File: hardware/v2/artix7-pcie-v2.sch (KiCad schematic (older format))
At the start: 34 parts, among them J10 USB_B_Micro, J3 JTAG_EN, J6 JTAG, J7 Conn_01x02, J8 SER0, J9 SER1, SW1 PROG, SW2 SW_SPST, U1 XC7A75T-FGG484, U2 W25Q64JVSSIM

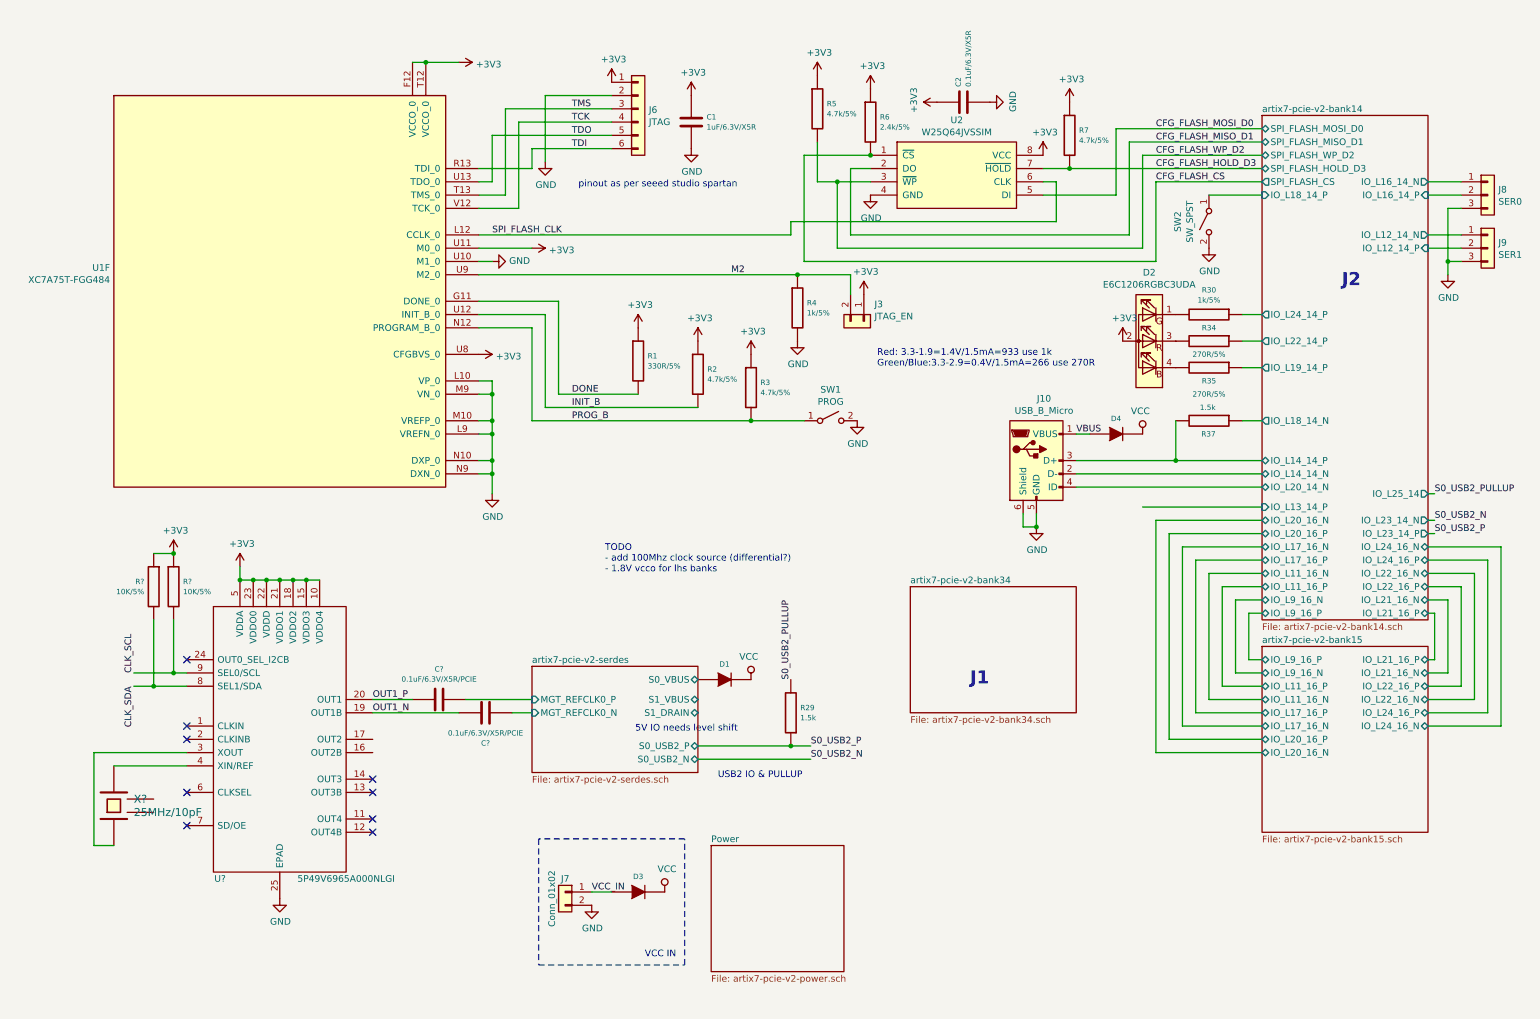
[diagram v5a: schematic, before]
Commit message: v2 pcb/schematic update : drc passing, need to add caps
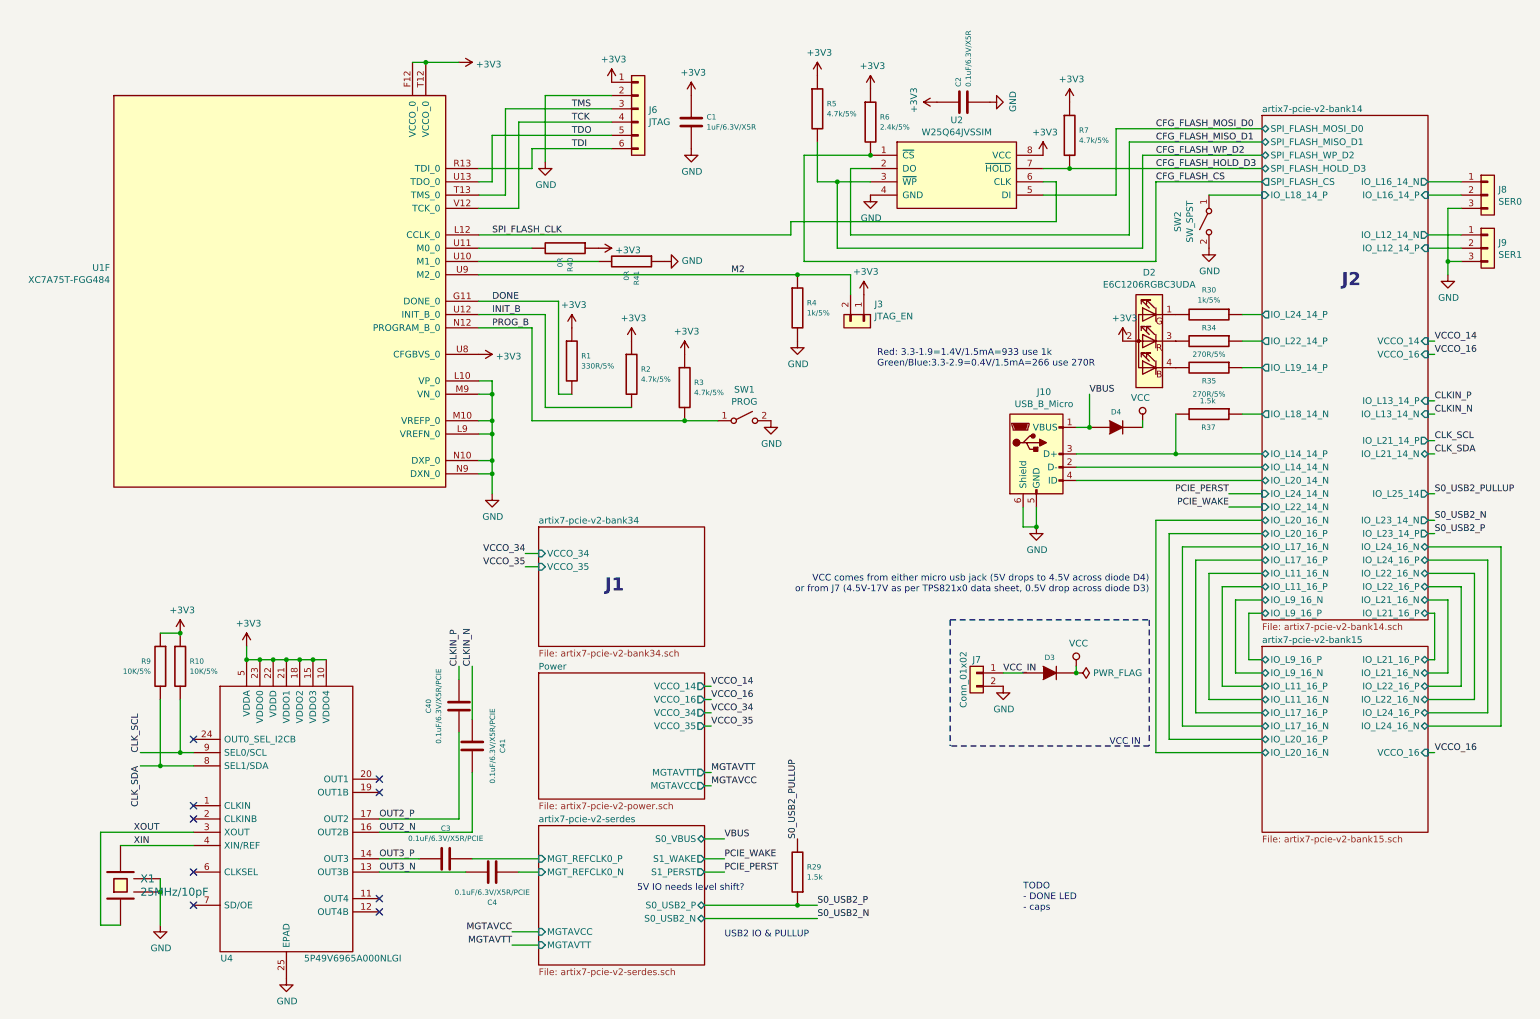
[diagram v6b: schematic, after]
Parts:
- removed D1: SBR3U20SA-13‎, tom-semiconductors:D_SMA, symbol tom-passives:DIODE
- added C40, C41: 0.1uF/6.3V/X5R/PCIE, tom-passives:C_0402_1005Metric, symbol tom-passives:C
- added R40, R41: 0R, tom-passives:C_0402_1005Metric, symbol tom-passives:R
- J6: footprint tom-connectors:PinHeader_1x06_P2.54mm_Vertical_SMD_Pin1Left -> tom-connectors:PinHeader_2x03_P2.54mm_Vertical
- U4: renamed from U?; footprint QFN50P400X400X100-25N-D -> artix7-pcie-v2:QFN50P400X400X100-25N-D
- gave numbers to parts that had none: 5
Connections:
- net +3V3: now also R40.1; no longer U1.U11 (M0_0)
- net GND: now also X1.2 (GND), X1.4 (GND), R41.1; no longer U1.U10 (M1_0)
- net OUT3_N: now reaches U4.13 (OUT3B)
- net OUT3_N: now also C4.1
- net OUT3_P: now reaches U4.14 (OUT3)
- net OUT3_P: now also C3.2
- net OUT2_N: now reaches U4.16 (OUT2B)
- net OUT2_N: now also C41.1
- net OUT2_P: now reaches U4.17 (OUT2)
- net OUT2_P: now also C40.2
- net XOUT: now reaches U4.3 (XOUT), X1.1
- net XIN: now reaches U4.4 (XIN/REF), X1.3
- net OUT1_N: no longer names the net of U4.19 (OUT1B)
- net OUT1_N: no longer C4.1
- net OUT1_P: no longer names the net of U4.20 (OUT1)
- net OUT1_P: no longer C3.2
- new net: R41.2, U1.U10 (M1_0)
- new net: R40.2, U1.U11 (M0_0)
- new net CLKIN_N: C41.2
- new net CLKIN_P: C40.1
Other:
- note added: "5V IO needs level shift?"
- note added: "TODO \n- DONE LED\n- caps"
- note added: "VCC comes from either micro usb jack (5V drops to 4.5V across diode D4)\nor from J7 (4.5V-17V as per TPS821x0 data sheet, 0.5V drop across diode D3)"
- note removed: "5V IO needs level shift"
- note removed: "TODO \n- add 100Mhz clock source (differential?)\n- 1.8V vcco for lhs banks"
- note removed: "pinout as per seeed studio spartan"
- moved on the sheet: C3, C4, D3, D4, J10, J7, R1, R10, R2, R29, R3, R37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

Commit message: v2 hardware: pcb progress commit, 155 unrouted
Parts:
- removed J8: SER0, tom-connectors:PinHeader_1x03_P2.54mm_Vertical, symbol tom-connectors:Conn_01x03
- removed J9: SER1, tom-connectors:PinHeader_1x03_P2.54mm_Vertical, symbol tom-connectors:Conn_01x03
- removed R40, R41: 0R, tom-passives:C_0402_1005Metric, symbol tom-passives:R
- added C17, C25, C27, C29, C31: 0.1uF/6.3V/X5R, tom-passives:C_0402_1005Metric, symbol tom-passives:C
- added D1: DONE, tom-passives:C_0402_1005Metric, symbol tom-opto:LED
- added D5: PWR, tom-passives:C_0402_1005Metric, symbol tom-opto:LED
- added J8: SER, tom-connectors:PinHeader_2x03_P2.54mm_Vertical, symbol tom-connectors:Conn_01x06
- added R51: 1K/5%, tom-passives:C_0402_1005Metric, symbol tom-passives:R
- added TP9: TestPoint, tom-mechanical:TestPoint_Loop_D2.50mm_Drill1.0mm, symbol tom-mechanical:TestPoint
- C1: value 1uF/6.3V/X5R -> 47uF/6.3V/X5R; footprint tom-passives:C_0402_1005Metric -> tom-passives:C_1206_3216Metric
- R1: value 330R/5% -> 1K/5%
- U2: footprint tom-semiconductors:SOIC-8_5.23x5.23mm_P1.27mm -> artix7-pcie-v2:WSON-8-1EP_8x6mm_P1.27mm
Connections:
- net +3V3: now also U1.U11 (M0_0), C17.1, C25.1, C27.1, C29.1, C31.1, R51.1
- net CLKIN_P: now also C40.2; no longer C40.1
- net DONE: now also D1.2 (A)
- net GND: now also U1.U10 (M1_0), C17.2, C25.2, C27.2, C29.2, C31.2, D1.1 (K), D5.1 (K), J8.1 (Pin_1), J8.2 (Pin_2), TP9.1
- net OUT2_P: now also C40.1; no longer C40.2
- net OUT3_P: now also C3.1; no longer C3.2
- net artix7-pcie-v2-bank14/IO_L12_14_N: now also J8.5 (Pin_5)
- net artix7-pcie-v2-bank14/IO_L12_14_P: now also J8.6 (Pin_6)
- net artix7-pcie-v2-bank14/IO_L16_14_N: now also J8.3 (Pin_3)
- net artix7-pcie-v2-bank14/IO_L16_14_P: now also J8.4 (Pin_4)
- net artix7-pcie-v2-serdes/MGT_REFCLK0_P: now also C3.2; no longer C3.1
- net artix7-pcie-v2-bank14/IO_L20_14_N renamed artix7-pcie-v2-bank14/IO_L11_14_P
- new net: D5.2 (A), R51.2
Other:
- note added: "Red Yeti Artix7 PCIe"
- note added: "TODO \n- POWER Good led\n- VCC led ?\n- caps for connectors (J1 and J2)\n- ps caps for clock chip"
- note added: "VCC comes from either micro usb jack (5V drops to approx 4V across diode D4)\nor from J7 (4V-17V as per TPS821x0 data sheet, 1V drop across diode D3)"
- note removed: "5V IO needs level shift?"
- note removed: "TODO \n- DONE LED\n- caps"
- note removed: "VCC comes from either micro usb jack (5V drops to 4.5V across diode D4)\nor from J7 (4.5V-17V as per TPS821x0 data sheet, 0.5V drop across diode D3)"
- moved on the sheet: C1

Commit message: v2 pcb/schematic progress commit, all tough signals routed out
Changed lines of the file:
@@
 F7 "MGTAVTT" I L 3900 7250 50
 F8 "MGTAVCC" I L 3900 7150 50
-F9 "S3_PERST" O R 5150 6700 50
-F10 "S3_WAKE" O R 5150 6600 50
+F9 "S2_PERST" O R 5150 6700 50
+F10 "S2_WAKE" O R 5150 6600 50
 $EndSheet
 Text Notes 5300 7200 0    50   ~ 0
@@
 F0 "artix7-pcie-v2-bank15" 50
 F1 "artix7-pcie-v2-bank15.sch" 50
-F2 "IO_L9_16_P" B L 9350 5100 50
-F3 "IO_L9_16_N" B L 9350 5200 50
-F4 "IO_L11_16_P" B L 9350 5300 50
-F5 "IO_L17_16_P" B L 9350 5500 50
-F6 "IO_L17_16_N" B L 9350 5600 50
-F7 "IO_L11_16_N" B L 9350 5400 50
-F8 "IO_L21_16_P" B R 10600 5100 50
-F9 "IO_L21_16_N" B R 10600 5200 50
-F10 "IO_L20_16_P" B L 9350 5700 50
-F11 "IO_L20_16_N" B L 9350 5800 50
-F12 "IO_L24_16_P" B R 10600 5500 50
-F13 "IO_L24_16_N" B R 10600 5600 50
-F14 "IO_L22_16_N" B R 10600 5400 50
-F15 "IO_L22_16_P" B R 10600 5300 50
-F16 "VCCO_16" I R 10600 5800 50
+F2 "IO_L11_16_P" B L 9350 5300 50
+F3 "IO_L17_16_P" B L 9350 5500 50
+F4 "IO_L17_16_N" B L 9350 5600 50
+F5 "IO_L11_16_N" B L 9350 5400 50
+F6 "IO_L21_16_P" B R 10600 5100 50
+F7 "IO_L21_16_N" B R 10600 5200 50
+F8 "IO_L20_16_P" B L 9350 5700 50
+F9 "IO_L20_16_N" B L 9350 5800 50
+F10 "IO_L24_16_P" B R 10600 5500 50
+F11 "IO_L24_16_N" B R 10600 5600 50
+F12 "IO_L22_16_N" B R 10600 5400 50
+F13 "IO_L22_16_P" B R 10600 5300 50
+F14 "VCCO_16" I R 10600 5800 50
+F15 "IO_L23_16_N" B L 9350 5200 50
+F16 "IO_L23_16_P" B L 9350 5100 50
 $EndSheet
 Wire Wire Line
@@
 F5 "SPI_FLASH_HOLD_D3" B L 9350 1400 50
 F6 "SPI_FLASH_CS" O L 9350 1500 50
-F7 "IO_L9_16_P" B L 9350 4750 50
-F8 "IO_L9_16_N" B L 9350 4650 50
-F9 "IO_L17_16_P" B L 9350 4350 50
-F10 "IO_L17_16_N" B L 9350 4250 50
-F11 "IO_L11_16_N" B L 9350 4450 50
-F12 "IO_L11_16_P" B L 9350 4550 50
-F13 "IO_L21_16_N" B R 10600 4650 50
-F14 "IO_L21_16_P" B R 10600 4750 50
-F15 "IO_L20_16_P" B L 9350 4150 50
-F16 "IO_L20_16_N" B L 9350 4050 50
-F17 "IO_L24_16_N" B R 10600 4250 50
-F18 "IO_L24_16_P" B R 10600 4350 50
-F19 "IO_L22_16_N" B R 10600 4450 50
-F20 "IO_L22_16_P" B R 10600 4550 50
-F21 "IO_L13_14_P" I R 10600 3150 50
-F22 "IO_L18_14_P" I L 9350 1600 50
-F23 "IO_L16_14_P" I R 10600 1600 50
-F24 "IO_L16_14_N" O R 10600 1500 50
-F25 "IO_L12_14_P" I R 10600 1800 50
-F26 "IO_L12_14_N" O R 10600 1700 50
-F27 "IO_L19_14_P" O L 9350 2900 50
-F28 "IO_L22_14_P" O L 9350 2700 50
-F29 "IO_L24_14_P" O L 9350 2500 50
-F30 "IO_L14_14_P" B L 9350 3550 50
-F31 "IO_L18_14_N" O L 9350 3250 50
-F32 "IO_L14_14_N" B L 9350 3650 50
-F33 "VCCO_14" I R 10600 2700 50
-F34 "VCCO_16" I R 10600 2800 50
-F35 "IO_L13_14_N" I R 10600 3250 50
-F36 "IO_L21_14_N" B R 10600 3550 50
-F37 "IO_L21_14_P" O R 10600 3450 50
-F38 "IO_L22_14_N" I L 9350 3950 50
-F39 "IO_L24_14_N" I L 9350 3850 50
-F40 "IO_L5_14_P" B R 10600 4150 50
-F41 "IO_L5_14_N" B R 10600 4050 50
-F42 "IO_L0_14" O R 10600 3850 50
-F43 "IO_L11_14_P" B L 9350 3750 50
+F7 "IO_L17_16_P" B L 9350 4350 50
+F8 "IO_L17_16_N" B L 9350 4250 50
+F9 "IO_L11_16_N" B L 9350 4450 50
+F10 "IO_L11_16_P" B L 9350 4550 50
+F11 "IO_L21_16_N" B R 10600 4650 50
+F12 "IO_L21_16_P" B R 10600 4750 50
+F13 "IO_L20_16_P" B L 9350 4150 50
+F14 "IO_L20_16_N" B L 9350 4050 50
+F15 "IO_L24_16_N" B R 10600 4250 50
+F16 "IO_L24_16_P" B R 10600 4350 50
+F17 "IO_L22_16_N" B R 10600 4450 50
+F18 "IO_L22_16_P" B R 10600 4550 50
+F19 "IO_L13_14_P" I R 10600 3150 50
+F20 "IO_L18_14_P" I L 9350 1600 50
+F21 "IO_L16_14_P" I R 10600 1600 50
+F22 "IO_L16_14_N" O R 10600 1500 50
+F23 "IO_L12_14_P" I R 10600 1800 50
+F24 "IO_L12_14_N" O R 10600 1700 50
+F25 "IO_L19_14_P" O L 9350 2900 50
+F26 "IO_L22_14_P" O L 9350 2700 50
+F27 "IO_L24_14_P" O L 9350 2500 50
+F28 "IO_L14_14_P" B L 9350 3550 50
+F29 "IO_L18_14_N" O L 9350 3250 50
+F30 "IO_L14_14_N" B L 9350 3650 50
+F31 "VCCO_14" I R 10600 2700 50
+F32 "VCCO_16" I R 10600 2800 50
+F33 "IO_L13_14_N" I R 10600 3250 50
+F34 "IO_L21_14_N" B R 10600 3550 50
+F35 "IO_L21_14_P" O R 10600 3450 50
+F36 "IO_L22_14_N" I L 9350 3950 50
+F37 "IO_L24_14_N" I L 9350 3850 50
+F38 "IO_L5_14_P" B R 10600 4150 50
+F39 "IO_L5_14_N" B R 10600 4050 50
+F40 "IO_L0_14" O R 10600 3850 50
+F41 "IO_L11_14_P" B L 9350 3750 50
+F42 "IO_L23_16_P" B L 9350 4750 50
+F43 "IO_L23_16_N" B L 9350 4650 50
 $EndSheet
 $Comp
